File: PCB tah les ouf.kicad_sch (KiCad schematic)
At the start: 24 parts, among them J1 USB_C_Receptacle_USB2.0_16P, SW1 SW_DIP_x02, SW2 SW_DIP_x02, SW3 SW_DIP_x02, SW4 SW_DIP_x02, U1 ESP32-S3-WROOM-1, U2 TMC2209_SILENTSTEPSTICK, U3 TMC2209_SILENTSTEPSTICK, U4 TMC2209_SILENTSTEPSTICK, U5 TMC2209_SILENTSTEPSTICK, U6 D3V3XA4B10LP, U7 AMS1117-3.3 (UMW)

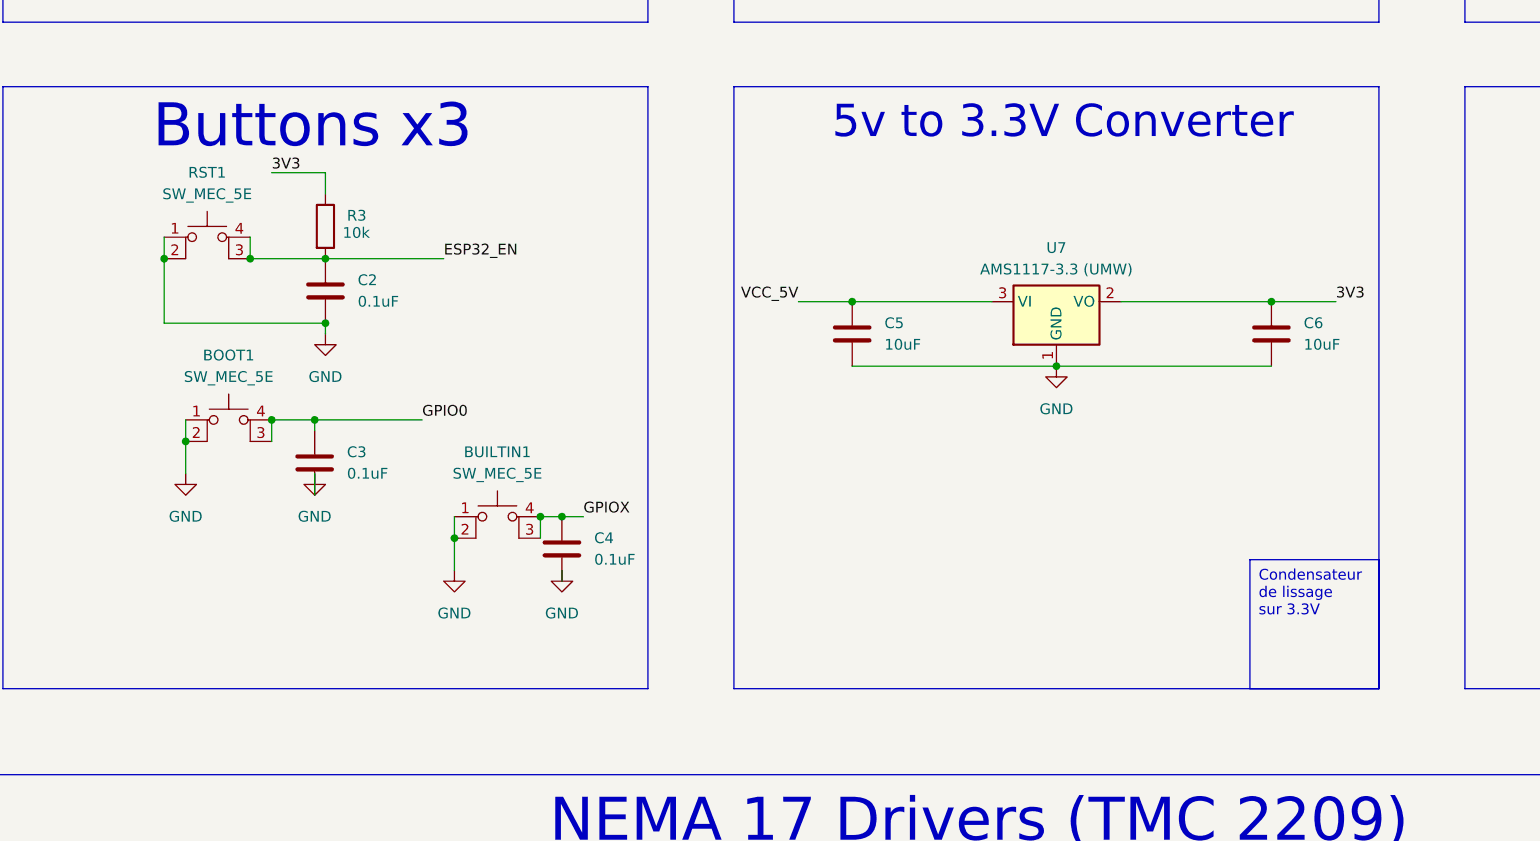
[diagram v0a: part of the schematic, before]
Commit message: Add buttons for reset, boot, and built-in functions
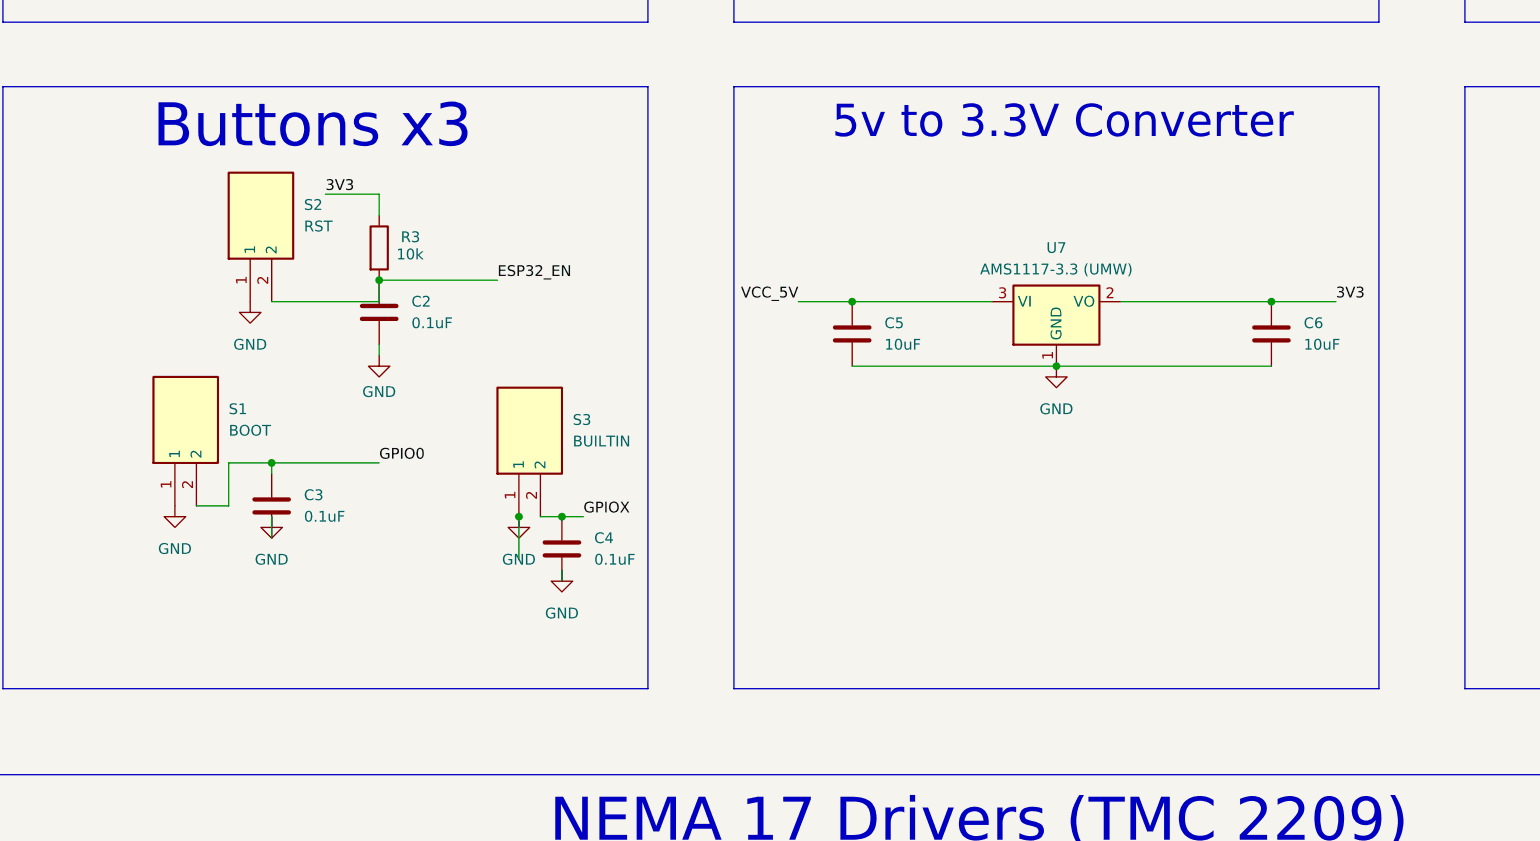
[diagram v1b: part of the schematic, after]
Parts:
- removed BOOT1, BUILTIN1, RST1: SW_MEC_5E, Button_Switch_THT:SW_PUSH_6mm_H4.3mm, symbol Switch:SW_MEC_5E
- added S1: BOOT, SKRKAEE020, symbol SKRKAEE020:SKRKAEE020
- added S2: RST, SKRKAEE020, symbol SKRKAEE020:SKRKAEE020
- added S3: BUILTIN, SKRKAEE020, symbol SKRKAEE020:SKRKAEE020
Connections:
- net ESP32_EN: now also S2.2
- net GND: now also S1.1, S2.1, S3.1
- net GPIO0: now also S1.2
- net GPIOX: now also S3.2
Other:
- moved on the sheet: C2, C3, R3

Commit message: Suppression TMC2209 x1
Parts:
- removed SW4: SW_DIP_x02, symbol Switch:SW_DIP_x02
- removed U5: TMC2209_SILENTSTEPSTICK, TMC2209:MODULE_TMC2209_SILENTSTEPSTICK, symbol TMC2209_SILENTSTEPSTICK:TMC2209_SILENTSTEPSTICK
- added ADD1, SCREEN1, TOF1, TOF2, TOF3: Conn_01x04_Pin, Connector_PinHeader_2.54mm:PinHeader_1x04_P2.54mm_Vertical, symbol Connector:Conn_01x04_Pin
- added D1, D2, D3: ~, Package_TO_SOT_THT:TO-18-2_Window, symbol LED:SFH482
- added R4, R5, R6: 1000, symbol Device:R
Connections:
- net GND: now also ADD1.4 (Pin_4), R4.2, R5.2, R6.2, SCREEN1.4 (Pin_4), TOF1.4 (Pin_4), TOF2.4 (Pin_4), TOF3.4 (Pin_4)
- net VCC_5V: now also ADD1.3 (Pin_3), D1.2 (A), D2.2 (A), D3.2 (A), SCREEN1.3 (Pin_3), TOF1.3 (Pin_3), TOF2.3 (Pin_3), TOF3.3 (Pin_3)
- net SDA: now reaches U1.10 (IO17)
- net SDA: now also ADD1.1 (Pin_1), SCREEN1.1 (Pin_1), TOF1.1 (Pin_1), TOF2.1 (Pin_1), TOF3.1 (Pin_1)
- net SCL: now reaches U1.11 (IO18)
- net SCL: now also ADD1.2 (Pin_2), SCREEN1.2 (Pin_2), TOF1.2 (Pin_2), TOF2.2 (Pin_2), TOF3.2 (Pin_2)
- new net: D2.1 (K), R5.1
- new net: D1.1 (K), R4.1
- new net: D3.1 (K), R6.1
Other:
- note added: "- BOOT Button - RESET Button - BUILTIN Button"
- note added: "- Protect when FLashing with USB-C - Protect when Default Power Delivery 5V/3A of PowerBank (No PD Control)"
- note added: "3x TMC2209 Drivers to control 3x NEMA 17 with 1A/phase each"
- note added: "5V to 3.3V/1A DC DC Converter"
- note added: "Builtin LED"
- note added: "Flash LED"
- note added: "GREEN = Done"
- note added: "I2C Protocol to control 4 Devices and 1 INPUT to add more"
- note added: "Normal Buzzer to make sound"
- note added: "ORANGE = Working"
- note added: "Power LED"
- note added: "RED = To start"
- note added: "TX and RX to control a LiDAR"
- note added: "USB-C used to flash ESP32 or to deliver power (Default 5V/ 3A No PD Control)"
- note added: "https://www.espressif.com/sites/default/files/documentation/esp32-s3_datasheet_en.pdf"
- note removed: "https://www.youtube.com/watch?v=KtPc4XwbiKA&ab_channel=BlagojeMrkic"
- moved on the sheet: J1, R1, R2, SW2, SW3, U3, U4

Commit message: Correction label + terminé i2c/uart
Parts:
- added TX0/RX0, TX1/RX1: Conn_01x04_Pin, Connector_PinHeader_2.54mm:PinHeader_1x04_P2.54mm_Vertical, symbol Connector:Conn_01x04_Pin
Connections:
- net ESP32_EN: no longer C2.1
- net GND: now also TOF1.3 (Pin_3), TOF2.3 (Pin_3), TOF3.3 (Pin_3), TX0/RX0.1 (Pin_1), TX1/RX1.1 (Pin_1); no longer TOF1.4 (Pin_4), TOF2.4 (Pin_4), TOF3.4 (Pin_4)
- net SCL: now also U1.38 (IO2); no longer U1.11 (IO18)
- net SDA: now also U1.15 (IO3); no longer U1.10 (IO17)
- net VCC_5V: now also TOF1.4 (Pin_4), TOF2.4 (Pin_4), TOF3.4 (Pin_4), TX0/RX0.4 (Pin_4), TX1/RX1.4 (Pin_4); no longer D2.2 (A), D3.2 (A), TOF1.3 (Pin_3), TOF2.3 (Pin_3), TOF3.3 (Pin_3)
- net UART_RX renamed RX0
- net RX0: now also TX0/RX0.2 (Pin_2)
- net UART_TX renamed TX0
- net TX0: now also TX0/RX0.3 (Pin_3)
- new net RX1: TX1/RX1.2 (Pin_2), U1.11 (IO18)
- new net TX1: TX1/RX1.3 (Pin_3), U1.10 (IO17)
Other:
- note added: "3x TMC2209 Drivers to control 3x NEMA 17 with 1A/phase each +Switch to control step"
- note added: "ORANGE = Working on"
- note added: "UART"
- note removed: "3x TMC2209 Drivers to control 3x NEMA 17 with 1A/phase each"
- note removed: "LiDAR"
- note removed: "ORANGE = Working"
- moved on the sheet: BZ1, C2
